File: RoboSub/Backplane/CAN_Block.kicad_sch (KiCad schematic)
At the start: 3 parts, among them U1 TCAN330G

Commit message: fix schematic
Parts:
- renumbered C1 to C8, C2 to C9, U1 to U3
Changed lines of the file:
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@@
     (effects (font (size 1.27 1.27)) (justify left))
   )
-  (symbol (lib_id "power:GND") (at 152.4 83.82 0) (unit 1)
+  (symbol (lib_id "power:GND") (at 152.4 83.82 0)
     (in_bom yes) (on_board yes)
-    (property "Reference" "#PWR?" (id 0) (at 152.4 90.17 0)
+    (property "Reference" "#PWR041" (id 0) (at 152.4 90.17 0)
       (effects (font (size 1.27 1.27)) hide)
     )
@@
     (pin "1")
   )
-  (symbol (lib_id "power:+3V3") (at 152.4 76.2 0) (unit 1)
+  (symbol (lib_id "power:+3V3") (at 152.4 76.2 0)
     (in_bom yes) (on_board yes)
-    (property "Reference" "#PWR?" (id 0) (at 152.4 80.01 0)
+    (property "Reference" "#PWR040" (id 0) (at 152.4 80.01 0)
       (effects (font (size 1.27 1.27)) hide)
     )
@@
     (pin "1")
   )
-  (symbol (lib_id "power:GND") (at 134.62 107.95 0) (unit 1)
+  (symbol (lib_id "power:GND") (at 134.62 107.95 0)
     (in_bom yes) (on_board yes)
-    (property "Reference" "#PWR?" (id 0) (at 134.62 114.3 0)
+    (property "Reference" "#PWR039" (id 0) (at 134.62 114.3 0)
       (effects (font (size 1.27 1.27)) hide)
     )
@@
     (pin "1")
   )
-  (symbol (lib_id "Device:C_Small") (at 152.4 80.01 0) (unit 1)
+  (symbol (lib_id "Device:C_Small") (at 152.4 80.01 0)
     (in_bom yes) (on_board yes)
-    (property "Reference" "C2" (id 0) (at 146.05 78.74 0)
+    (property "Reference" "C9" (id 0) (at 146.05 78.74 0)
       (effects (font (size 1.27 1.27)) (justify left))
     )
@@
     (pin "2")
   )
-  (symbol (lib_id "Device:C_Small") (at 143.51 80.01 0) (unit 1)
+  (symbol (lib_id "Device:C_Small") (at 143.51 80.01 0)
     (in_bom yes) (on_board yes)
-    (property "Reference" "C1" (id 0) (at 137.16 78.74 0)
+    (property "Reference" "C8" (id 0) (at 137.16 78.74 0)
       (effects (font (size 1.27 1.27)) (justify left))
     )
@@
     (pin "2")
   )
-  (symbol (lib_id "Interface_CAN_LIN:TCAN330G") (at 134.62 97.79 0) (unit 1)
+  (symbol (lib_id "Interface_CAN_LIN:TCAN330G") (at 134.62 97.79 0)
     (in_bom yes) (on_board yes)
-    (property "Reference" "U1" (id 0) (at 124.46 86.36 0))
+    (property "Reference" "U3" (id 0) (at 124.46 86.36 0))
     (property "Value" "TCAN330G" (id 1) (at 127 88.9 0))
     (property "Footprint" "Package_SO:SOIC-8_3.9x4.9mm_P1.27mm" (id 2) (at 134.62 110.49 0)

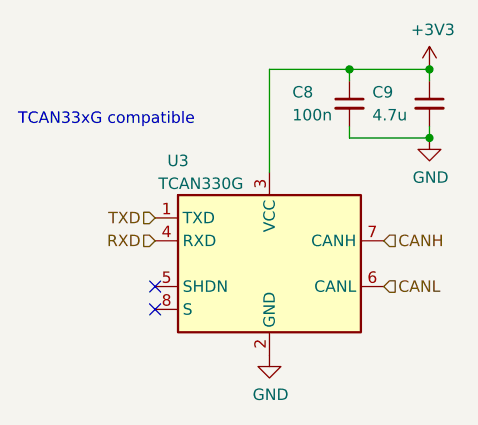
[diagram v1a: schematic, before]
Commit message: first backplane layout commit
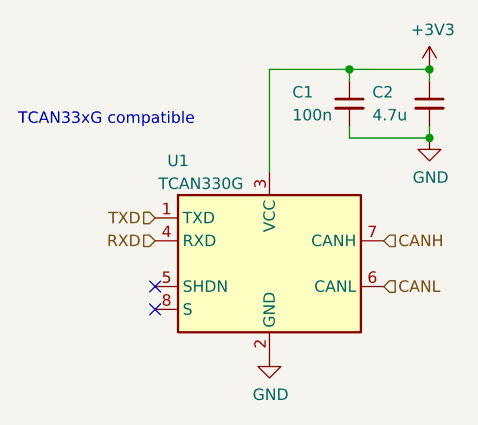
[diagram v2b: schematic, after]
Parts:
- renumbered C8 to C1, C9 to C2, U3 to U1
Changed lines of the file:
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@@
   (symbol (lib_id "Device:C_Small") (at 152.4 80.01 0)
     (in_bom yes) (on_board yes)
-    (property "Reference" "C9" (id 0) (at 146.05 78.74 0)
+    (property "Reference" "C2" (id 0) (at 146.05 78.74 0)
       (effects (font (size 1.27 1.27)) (justify left))
     )
@@
   (symbol (lib_id "Device:C_Small") (at 143.51 80.01 0)
     (in_bom yes) (on_board yes)
-    (property "Reference" "C8" (id 0) (at 137.16 78.74 0)
+    (property "Reference" "C1" (id 0) (at 137.16 78.74 0)
       (effects (font (size 1.27 1.27)) (justify left))
     )
@@
   (symbol (lib_id "Interface_CAN_LIN:TCAN330G") (at 134.62 97.79 0)
     (in_bom yes) (on_board yes)
-    (property "Reference" "U3" (id 0) (at 124.46 86.36 0))
+    (property "Reference" "U1" (id 0) (at 124.46 86.36 0))
     (property "Value" "TCAN330G" (id 1) (at 127 88.9 0))
     (property "Footprint" "Package_SO:SOIC-8_3.9x4.9mm_P1.27mm" (id 2) (at 134.62 110.49 0)

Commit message: made changes to blackplane layout second commit
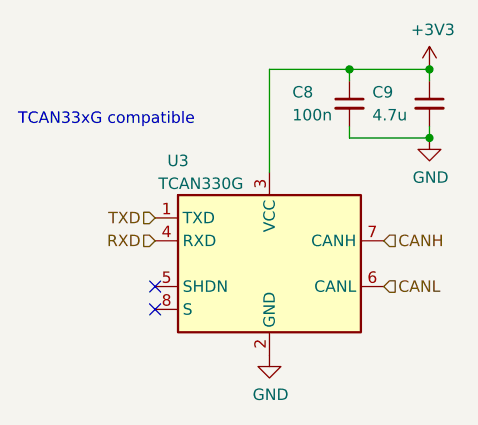
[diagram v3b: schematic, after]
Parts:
- renumbered C1 to C8, C2 to C9, U1 to U3
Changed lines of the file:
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@@
   (symbol (lib_id "Device:C_Small") (at 152.4 80.01 0)
     (in_bom yes) (on_board yes)
-    (property "Reference" "C2" (id 0) (at 146.05 78.74 0)
+    (property "Reference" "C9" (id 0) (at 146.05 78.74 0)
       (effects (font (size 1.27 1.27)) (justify left))
     )
@@
   (symbol (lib_id "Device:C_Small") (at 143.51 80.01 0)
     (in_bom yes) (on_board yes)
-    (property "Reference" "C1" (id 0) (at 137.16 78.74 0)
+    (property "Reference" "C8" (id 0) (at 137.16 78.74 0)
       (effects (font (size 1.27 1.27)) (justify left))
     )
@@
   (symbol (lib_id "Interface_CAN_LIN:TCAN330G") (at 134.62 97.79 0)
     (in_bom yes) (on_board yes)
-    (property "Reference" "U1" (id 0) (at 124.46 86.36 0))
+    (property "Reference" "U3" (id 0) (at 124.46 86.36 0))
     (property "Value" "TCAN330G" (id 1) (at 127 88.9 0))
     (property "Footprint" "Package_SO:SOIC-8_3.9x4.9mm_P1.27mm" (id 2) (at 134.62 110.49 0)

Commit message: add libs
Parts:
- renumbered C8 to C1, C9 to C2, U3 to U1
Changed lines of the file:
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@@
   (symbol (lib_id "power:GND") (at 152.4 83.82 0)
     (in_bom yes) (on_board yes)
-    (property "Reference" "#PWR041" (id 0) (at 152.4 90.17 0)
+    (property "Reference" "#PWR032" (id 0) (at 152.4 90.17 0)
       (effects (font (size 1.27 1.27)) hide)
     )
@@
   (symbol (lib_id "power:+3V3") (at 152.4 76.2 0)
     (in_bom yes) (on_board yes)
-    (property "Reference" "#PWR040" (id 0) (at 152.4 80.01 0)
+    (property "Reference" "#PWR031" (id 0) (at 152.4 80.01 0)
       (effects (font (size 1.27 1.27)) hide)
     )
@@
   (symbol (lib_id "power:GND") (at 134.62 107.95 0)
     (in_bom yes) (on_board yes)
-    (property "Reference" "#PWR039" (id 0) (at 134.62 114.3 0)
+    (property "Reference" "#PWR030" (id 0) (at 134.62 114.3 0)
       (effects (font (size 1.27 1.27)) hide)
     )
@@
   (symbol (lib_id "Device:C_Small") (at 152.4 80.01 0)
     (in_bom yes) (on_board yes)
-    (property "Reference" "C9" (id 0) (at 146.05 78.74 0)
+    (property "Reference" "C2" (id 0) (at 146.05 78.74 0)
       (effects (font (size 1.27 1.27)) (justify left))
     )
@@
   (symbol (lib_id "Device:C_Small") (at 143.51 80.01 0)
     (in_bom yes) (on_board yes)
-    (property "Reference" "C8" (id 0) (at 137.16 78.74 0)
+    (property "Reference" "C1" (id 0) (at 137.16 78.74 0)
       (effects (font (size 1.27 1.27)) (justify left))
     )
@@
   (symbol (lib_id "Interface_CAN_LIN:TCAN330G") (at 134.62 97.79 0)
     (in_bom yes) (on_board yes)
-    (property "Reference" "U3" (id 0) (at 124.46 86.36 0))
+    (property "Reference" "U1" (id 0) (at 124.46 86.36 0))
     (property "Value" "TCAN330G" (id 1) (at 127 88.9 0))
     (property "Footprint" "Package_SO:SOIC-8_3.9x4.9mm_P1.27mm" (id 2) (at 134.62 110.49 0)

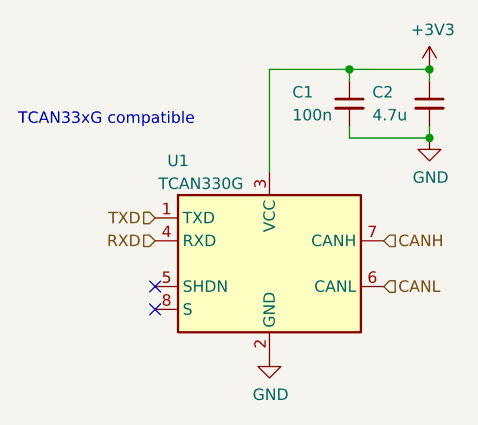
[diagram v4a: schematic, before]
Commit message: layout placement done, haven't connect nets
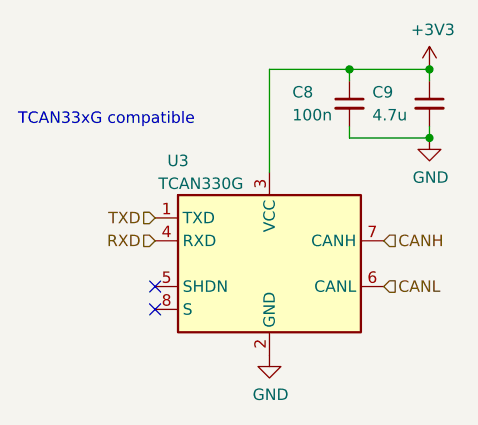
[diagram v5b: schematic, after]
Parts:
- renumbered C1 to C8, C2 to C9, U1 to U3
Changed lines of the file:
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@@
   (symbol (lib_id "power:GND") (at 152.4 83.82 0)
     (in_bom yes) (on_board yes)
-    (property "Reference" "#PWR032" (id 0) (at 152.4 90.17 0)
+    (property "Reference" "#PWR041" (id 0) (at 152.4 90.17 0)
       (effects (font (size 1.27 1.27)) hide)
     )
@@
   (symbol (lib_id "power:+3V3") (at 152.4 76.2 0)
     (in_bom yes) (on_board yes)
-    (property "Reference" "#PWR031" (id 0) (at 152.4 80.01 0)
+    (property "Reference" "#PWR040" (id 0) (at 152.4 80.01 0)
       (effects (font (size 1.27 1.27)) hide)
     )
@@
   (symbol (lib_id "power:GND") (at 134.62 107.95 0)
     (in_bom yes) (on_board yes)
-    (property "Reference" "#PWR030" (id 0) (at 134.62 114.3 0)
+    (property "Reference" "#PWR039" (id 0) (at 134.62 114.3 0)
       (effects (font (size 1.27 1.27)) hide)
     )
@@
   (symbol (lib_id "Device:C_Small") (at 152.4 80.01 0)
     (in_bom yes) (on_board yes)
-    (property "Reference" "C2" (id 0) (at 146.05 78.74 0)
+    (property "Reference" "C9" (id 0) (at 146.05 78.74 0)
       (effects (font (size 1.27 1.27)) (justify left))
     )
@@
   (symbol (lib_id "Device:C_Small") (at 143.51 80.01 0)
     (in_bom yes) (on_board yes)
-    (property "Reference" "C1" (id 0) (at 137.16 78.74 0)
+    (property "Reference" "C8" (id 0) (at 137.16 78.74 0)
       (effects (font (size 1.27 1.27)) (justify left))
     )
@@
   (symbol (lib_id "Interface_CAN_LIN:TCAN330G") (at 134.62 97.79 0)
     (in_bom yes) (on_board yes)
-    (property "Reference" "U1" (id 0) (at 124.46 86.36 0))
+    (property "Reference" "U3" (id 0) (at 124.46 86.36 0))
     (property "Value" "TCAN330G" (id 1) (at 127 88.9 0))
     (property "Footprint" "Package_SO:SOIC-8_3.9x4.9mm_P1.27mm" (id 2) (at 134.62 110.49 0)
